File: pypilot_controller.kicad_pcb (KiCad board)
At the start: 4 copper layers, 76.6 x 50.6 mm, 82 parts, among them J1 power+, J2 power-, J3 power+, J4 power+, J5 UART_Device, J6 Rudder, J7 End Stops, J8 Conn_01x02, J9 ISP, Q1 Q_NMOS_GDS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

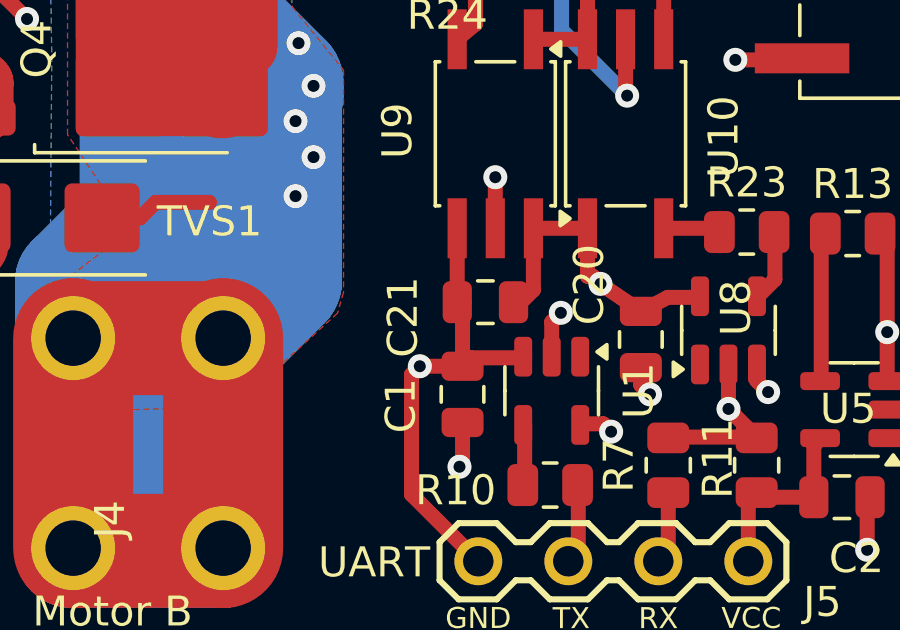
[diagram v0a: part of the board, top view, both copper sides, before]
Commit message: Fix a courtyard clearance problem
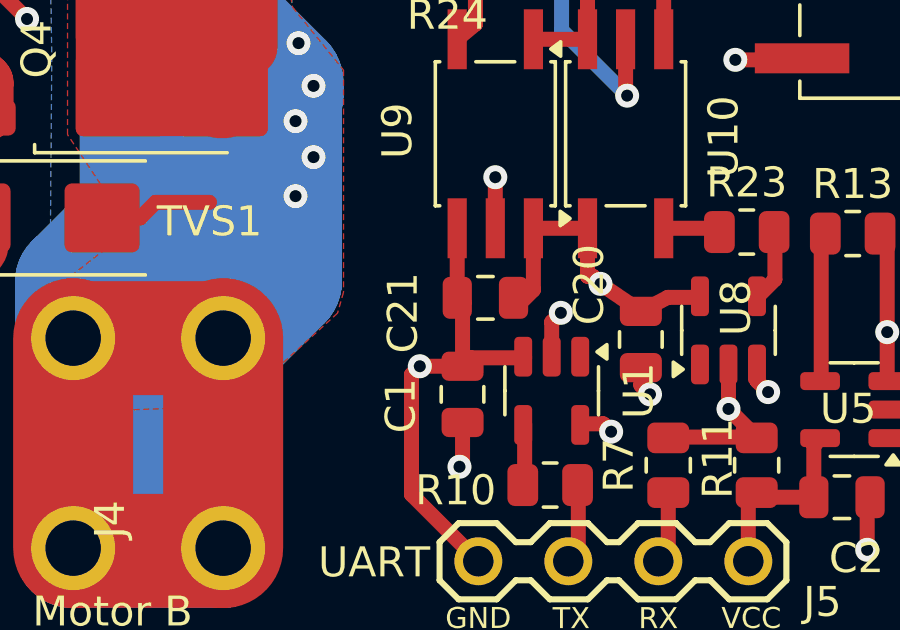
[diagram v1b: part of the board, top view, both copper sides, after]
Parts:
- moved C21 0.14 mm to (59.0, 40.1)
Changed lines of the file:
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@@
 	(footprint "Capacitor_SMD:C_0805_2012Metric"
 		(layer "F.Cu")
-		(at 58.9788 40.2844 180)
+		(at 58.9788 40.14 180)
 		(descr "Capacitor SMD 0805 (2012 Metric), square (rectangular) end terminal, IPC_7351 nominal, (Body size source: https://docs.google.com/spreadsheets/d/1BsfQQcO9C6DZCsRaXUlFlo91Tg2WpOkGARC1WS5S8t0/edit?usp=sharing), generated with kicad-footprint-generator")
 		(tags "capacitor")

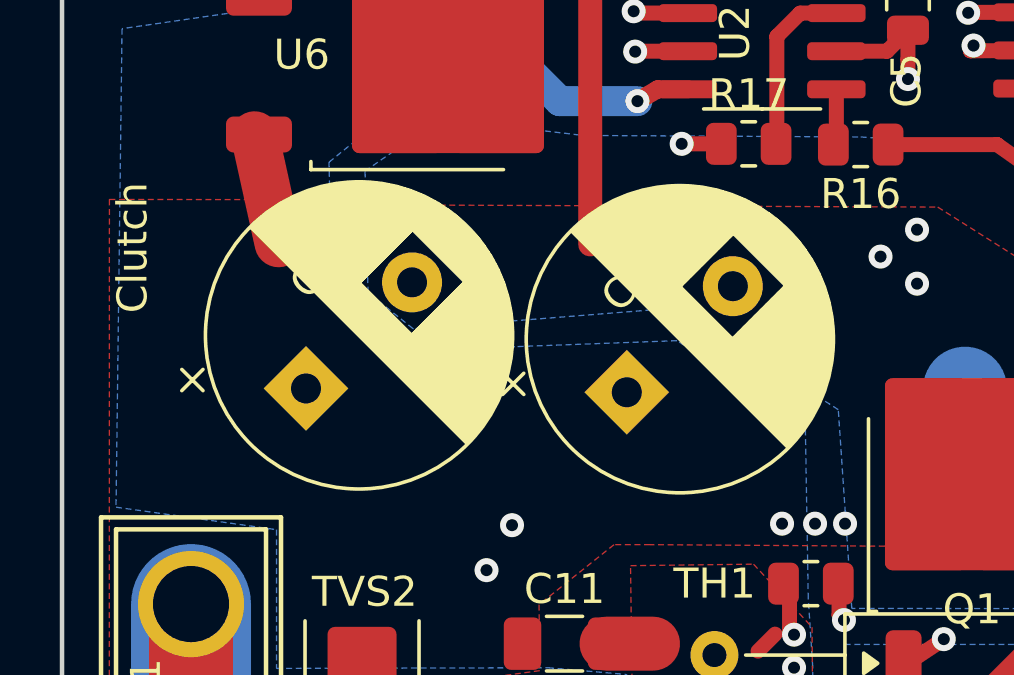
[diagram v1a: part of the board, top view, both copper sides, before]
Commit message: Update footprints on PCB for electrolytics
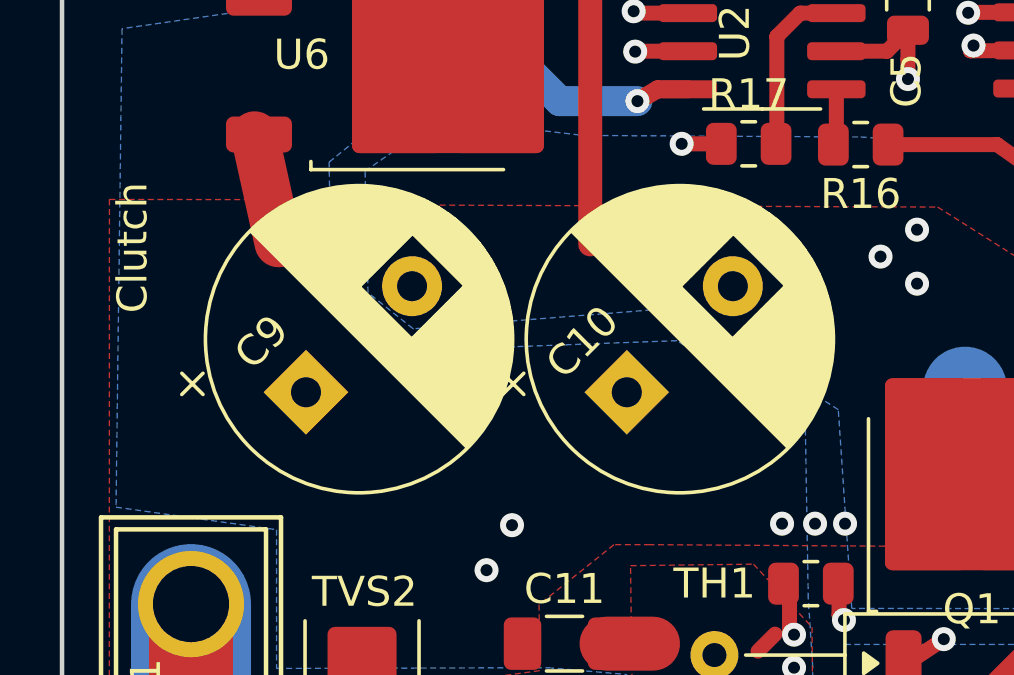
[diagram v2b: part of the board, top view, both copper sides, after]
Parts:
- moved C9 2.59 mm to (9.98, 20.3)
- moved C10 2.50 mm to (20.7, 20.3)

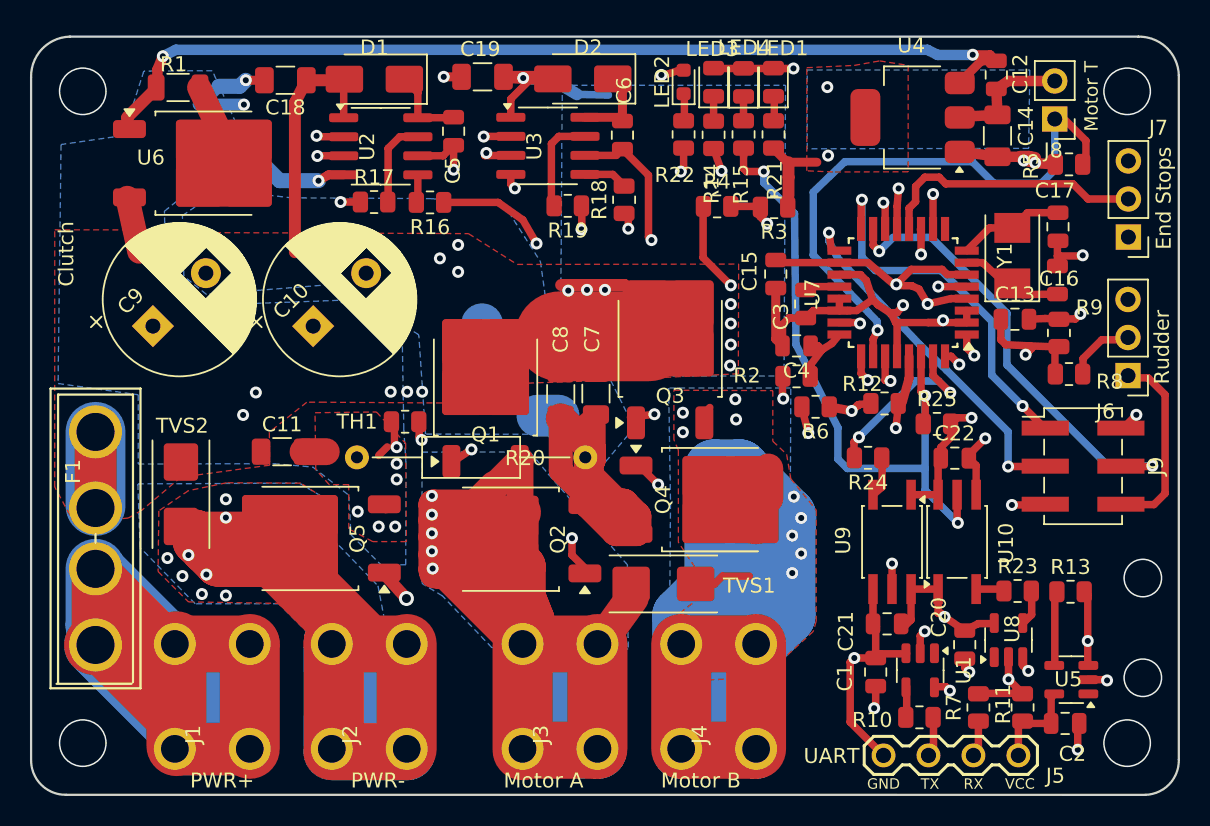
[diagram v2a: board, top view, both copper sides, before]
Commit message: Update footprints on PCB for 1206 capacitors
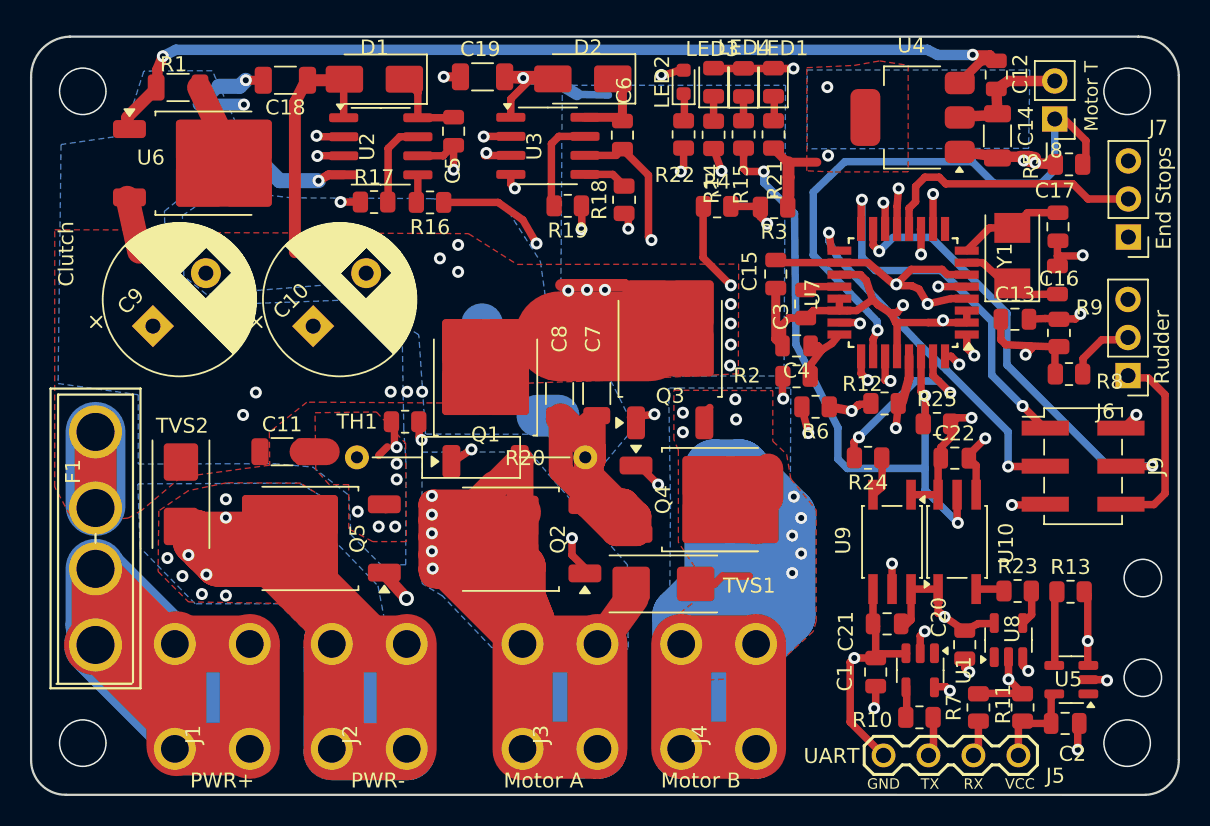
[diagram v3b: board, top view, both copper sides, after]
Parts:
- moved C8 0.08 mm to (37.1, 24.8)
- moved C7 0.05 mm to (39.6, 24.8)

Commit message: Update footprints on PCB for 0805 caps
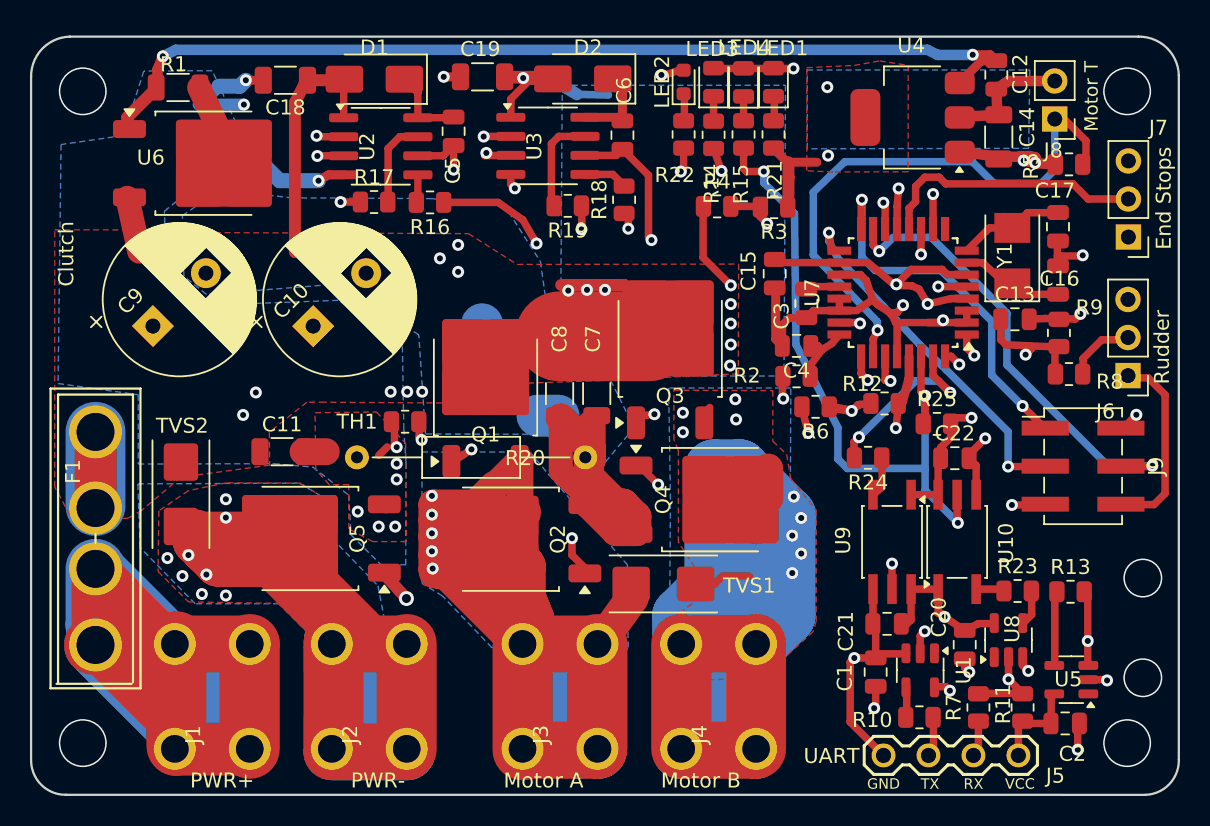
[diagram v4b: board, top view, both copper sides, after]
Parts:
- moved C14 0.11 mm to (66.4, 7.64)
- moved C15 0.07 mm to (51.5, 16.8)
- moved C3 0.06 mm to (53.6, 18.8)
